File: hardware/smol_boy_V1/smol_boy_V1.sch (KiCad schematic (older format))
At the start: 21 parts, among them J1 Conn_01x01_Male, J2 Conn_01x06_Male, J3 Conn_01x04_Male, J4 Conn_01x03_Male, J5 Conn_01x03_Male, J6 Conn_01x03_Male, J7 Conn_01x03_Male, J8 Conn_01x03_Male, J9 Conn_01x03_Male, U1 ESP-12E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

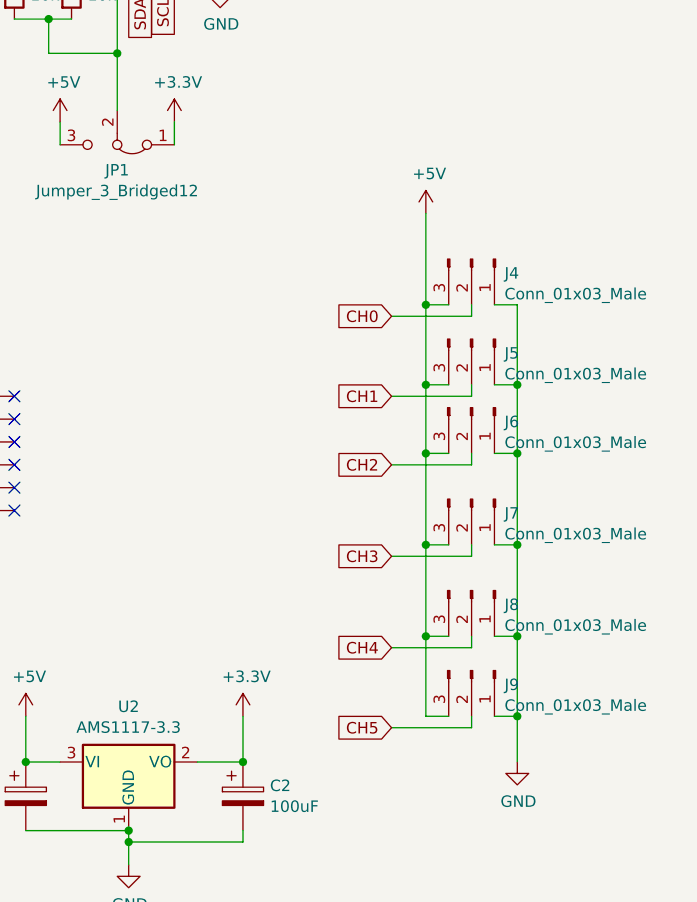
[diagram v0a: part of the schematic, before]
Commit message: fixed pcb channel pins
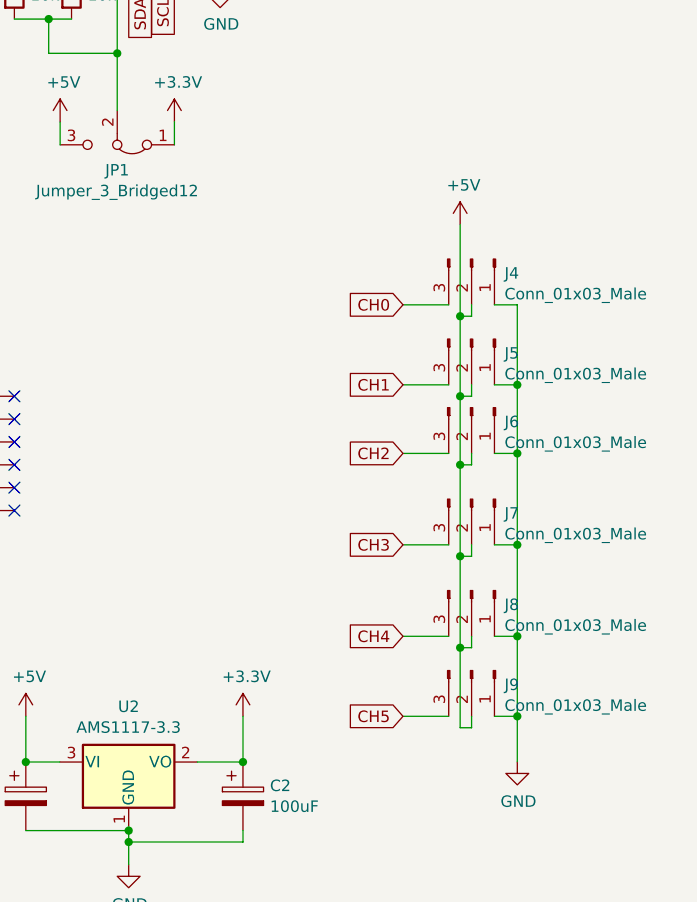
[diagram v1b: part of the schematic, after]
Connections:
- net +5V: now also J4.2 (Pin_2), J5.2 (Pin_2), J6.2 (Pin_2), J7.2 (Pin_2), J8.2 (Pin_2), J9.2 (Pin_2); no longer J4.3 (Pin_3), J5.3 (Pin_3), J6.3 (Pin_3), J7.3 (Pin_3), J8.3 (Pin_3), J9.3 (Pin_3)
- net CH0: now also J4.3 (Pin_3); no longer J4.2 (Pin_2)
- net CH1: now also J5.3 (Pin_3); no longer J5.2 (Pin_2)
- net CH2: now also J6.3 (Pin_3); no longer J6.2 (Pin_2)
- net CH3: now also J7.3 (Pin_3); no longer J7.2 (Pin_2)
- net CH4: now also J8.3 (Pin_3); no longer J8.2 (Pin_2)
- net CH5: now also J9.3 (Pin_3); no longer J9.2 (Pin_2)
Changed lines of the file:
@@
 	6050 5100 6050 4900
 Connection ~ 6050 4900
-Wire Wire Line
-	5750 4900 5650 4900
-Wire Wire Line
-	5650 4900 5650 4550
-Wire Wire Line
-	5650 3100 5750 3100
-Wire Wire Line
-	5650 3450 5750 3450
-Connection ~ 5650 3450
-Wire Wire Line
-	5650 3450 5650 3100
-Wire Wire Line
-	5650 3750 5750 3750
-Connection ~ 5650 3750
-Wire Wire Line
-	5650 3750 5650 3450
-Wire Wire Line
-	5650 4150 5750 4150
-Connection ~ 5650 4150
-Wire Wire Line
-	5650 4150 5650 3750
-Wire Wire Line
-	5650 4550 5750 4550
-Connection ~ 5650 4550
-Wire Wire Line
-	5650 4550 5650 4150
 $Comp
 L power:+5V #PWR0102
 U 1 1 5DF0AB13
-P 5650 2700
-F 0 "#PWR0102" H 5650 2550 50  0001 C CNN
-F 1 "+5V" H 5665 2873 50  0000 C CNN
-F 2 "" H 5650 2700 50  0001 C CNN
-F 3 "" H 5650 2700 50  0001 C CNN
-	1    5650 2700
-	1    0    0    -1
-$EndComp
-Wire Wire Line
-	5650 3100 5650 2700
-Connection ~ 5650 3100
+P 5800 2750
+F 0 "#PWR0102" H 5800 2600 50  0001 C CNN
+F 1 "+5V" H 5815 2923 50  0000 C CNN
+F 2 "" H 5800 2750 50  0001 C CNN
+F 3 "" H 5800 2750 50  0001 C CNN
+	1    5800 2750
+	1    0    0    -1
+$EndComp
 $Comp
 L power:GND #PWR0103
@@
 Wire Wire Line
 	2650 4750 2650 4650
-Text GLabel 5500 3150 0    50   Input ~ 0
+Text GLabel 5550 3100 0    50   Input ~ 0
 CH0
-Text GLabel 5500 3500 0    50   Input ~ 0
+Text GLabel 5550 3450 0    50   Input ~ 0
 CH1
-Text GLabel 5500 3800 0    50   Input ~ 0
+Text GLabel 5550 3750 0    50   Input ~ 0
 CH2
-Text GLabel 5500 4200 0    50   Input ~ 0
+Text GLabel 5550 4150 0    50   Input ~ 0
 CH3
-Text GLabel 5500 4600 0    50   Input ~ 0
+Text GLabel 5550 4550 0    50   Input ~ 0
 CH4
-Text GLabel 5500 4950 0    50   Input ~ 0
+Text GLabel 5550 4900 0    50   Input ~ 0
 CH5
 Text GLabel 4400 1700 3    50   Input ~ 0
@@
 SCL
 Wire Wire Line
-	5500 3150 5850 3150
-Wire Wire Line
 	5850 3150 5850 3100
 Wire Wire Line
-	5500 3500 5850 3500
-Wire Wire Line
 	5850 3500 5850 3450
 Wire Wire Line
-	5500 3800 5850 3800
-Wire Wire Line
 	5850 3800 5850 3750
 Wire Wire Line
-	5500 4200 5850 4200
-Wire Wire Line
 	5850 4200 5850 4150
 Wire Wire Line
-	5500 4600 5850 4600
-Wire Wire Line
 	5850 4600 5850 4550
-Wire Wire Line
-	5500 4950 5850 4950
 Wire Wire Line
 	5850 4950 5850 4900
@@
 Wire Wire Line
 	3850 1350 3850 1550
+Wire Wire Line
+	5850 4950 5800 4950
+Wire Wire Line
+	5800 4950 5800 4600
+Wire Wire Line
+	5850 3150 5800 3150
+Connection ~ 5800 3150
+Wire Wire Line
+	5800 3150 5800 2750
+Wire Wire Line
+	5850 3500 5800 3500
+Connection ~ 5800 3500
+Wire Wire Line
+	5800 3500 5800 3150
+Wire Wire Line
+	5850 3800 5800 3800
+Connection ~ 5800 3800
+Wire Wire Line
+	5800 3800 5800 3500
+Wire Wire Line
+	5850 4200 5800 4200
+Connection ~ 5800 4200
+Wire Wire Line
+	5800 4200 5800 3800
+Wire Wire Line
+	5850 4600 5800 4600
+Connection ~ 5800 4600
+Wire Wire Line
+	5800 4600 5800 4200
+Wire Wire Line
+	5550 3100 5750 3100
+Wire Wire Line
+	5550 3450 5750 3450
+Wire Wire Line
+	5550 3750 5750 3750
+Wire Wire Line
+	5550 4150 5750 4150
+Wire Wire Line
+	5550 4550 5750 4550
+Wire Wire Line
+	5550 4900 5750 4900
 $EndSCHEMATC

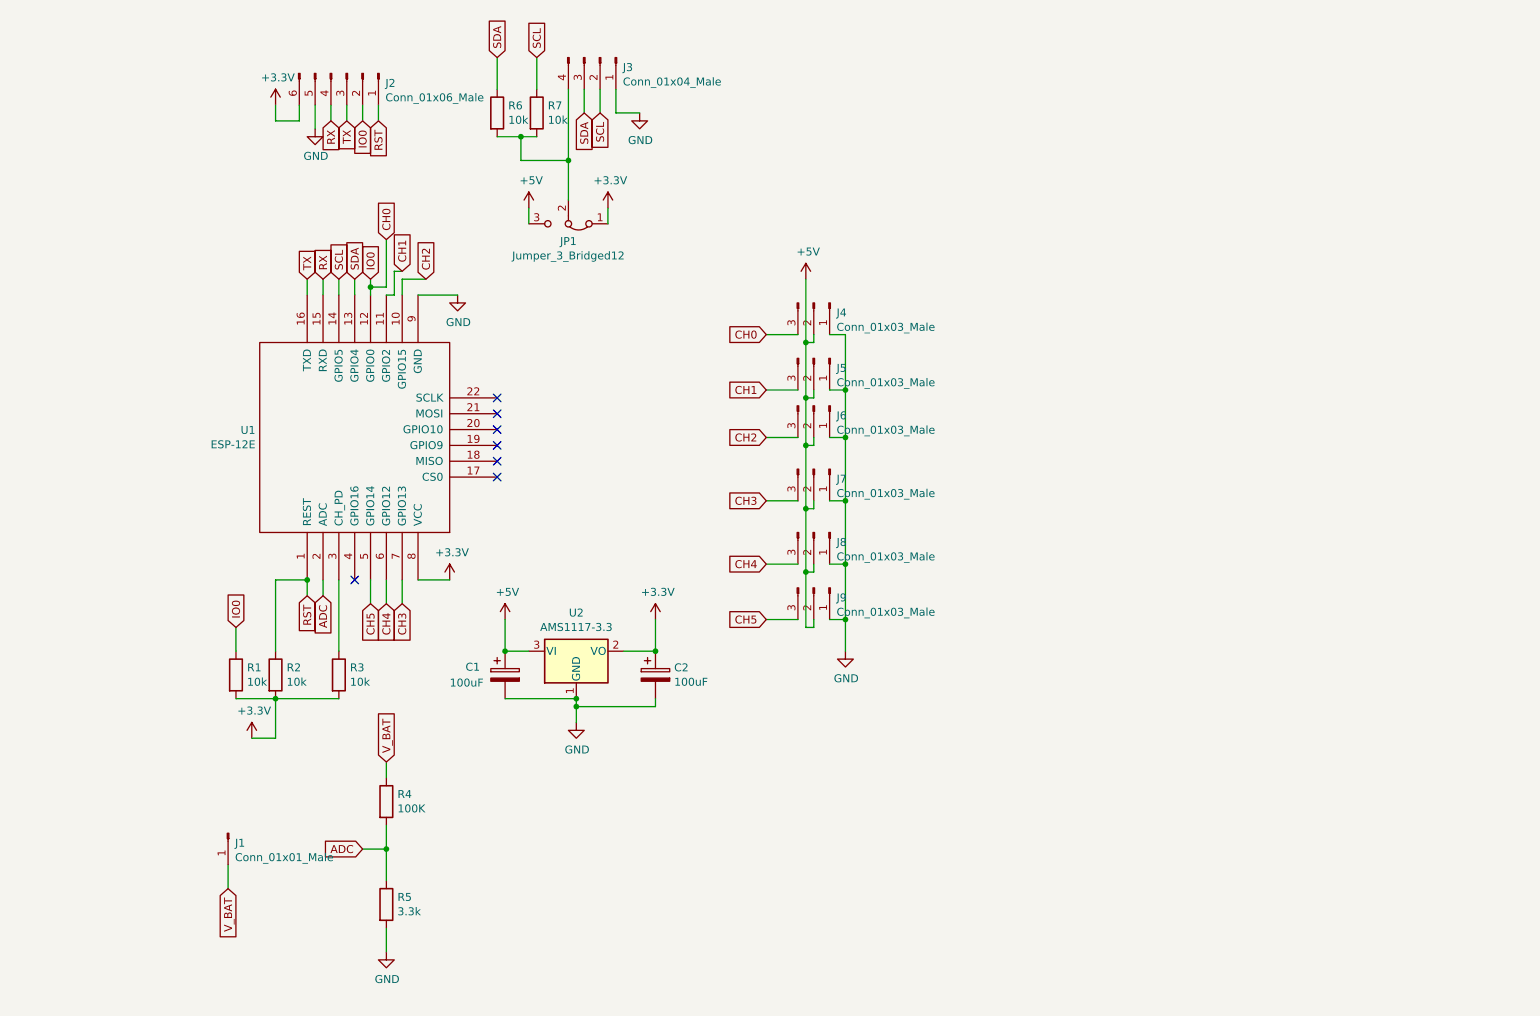
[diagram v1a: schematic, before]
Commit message: pcb pullups fixed
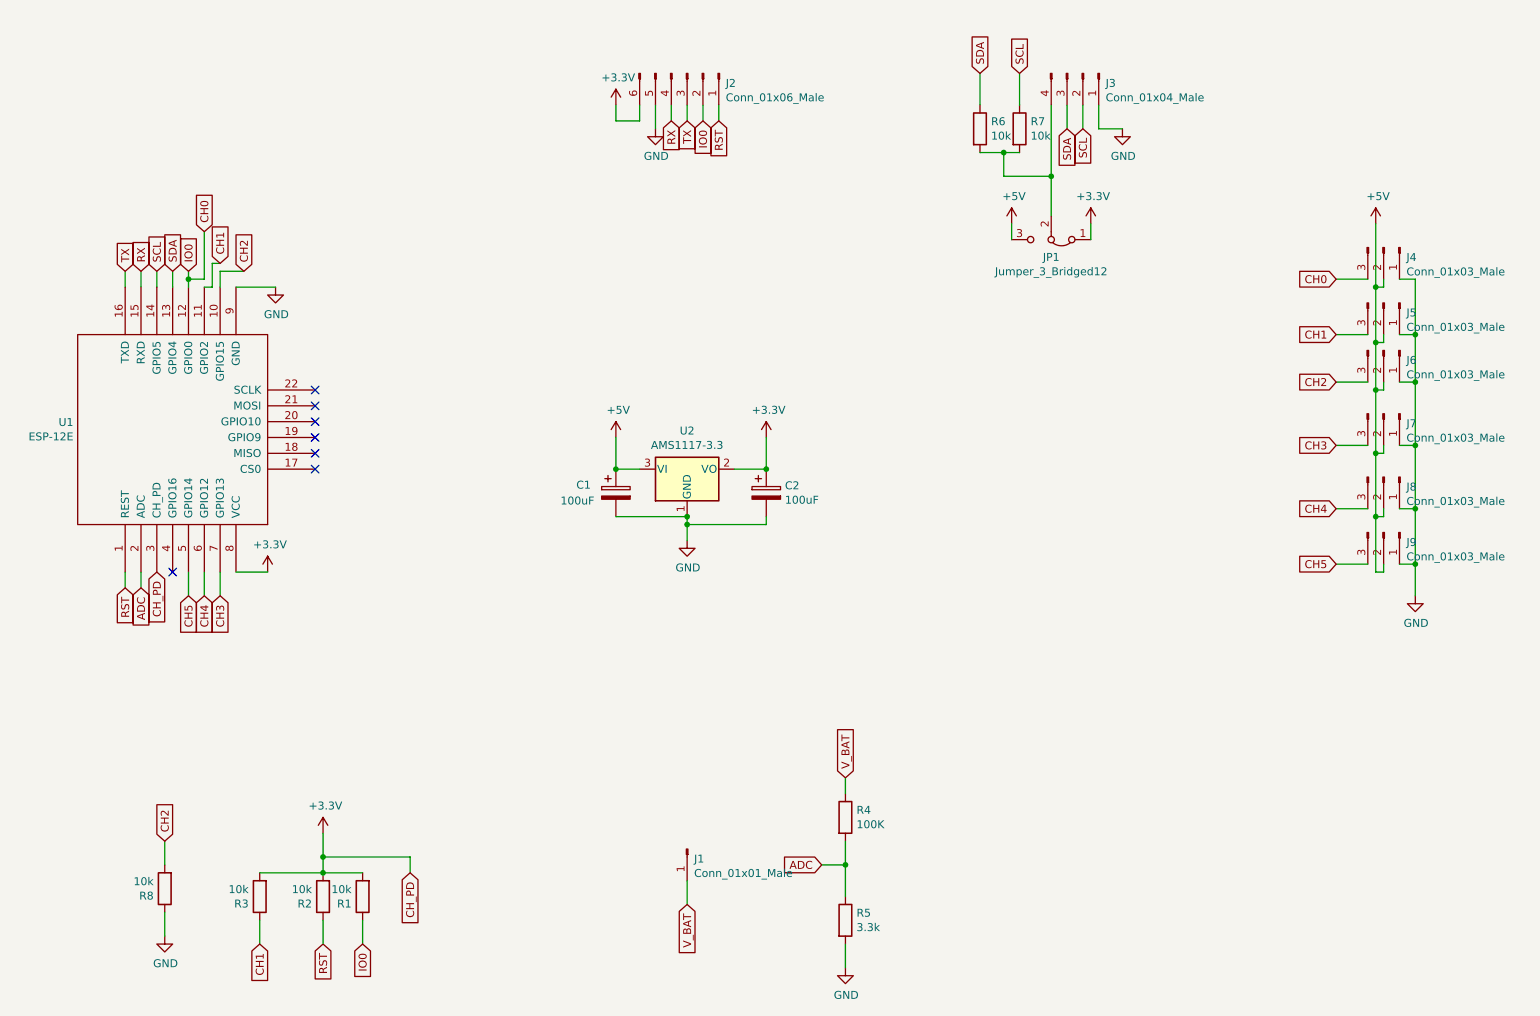
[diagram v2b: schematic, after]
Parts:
- added R3: 10k, Resistor_SMD:R_1206_3216Metric_Pad1.42x1.75mm_HandSolder, symbol Device:R
- renumbered R3 to R8
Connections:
- net +3V3: now also U1.3 (CH_PD), R3.2; no longer R8.2
- net CH1: now also R3.1
- net CH2: now also R8.2
- net GND: now also R8.1
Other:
- moved on the sheet: C1, C2, J1, J2, J3, J4, J5, J6, J7, J8, J9, JP1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
